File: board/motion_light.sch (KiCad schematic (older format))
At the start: 19 parts, among them CON1 AVR-ISP-6, J1 MOTION, J2 Conn_01x05, J3 USB_MICRO, J4 USB_MICRO, Q1 BSS83P, SW1 SW_Push, SW2 SW_Push, U1 ATTINY84A-SSU, U2 APA102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

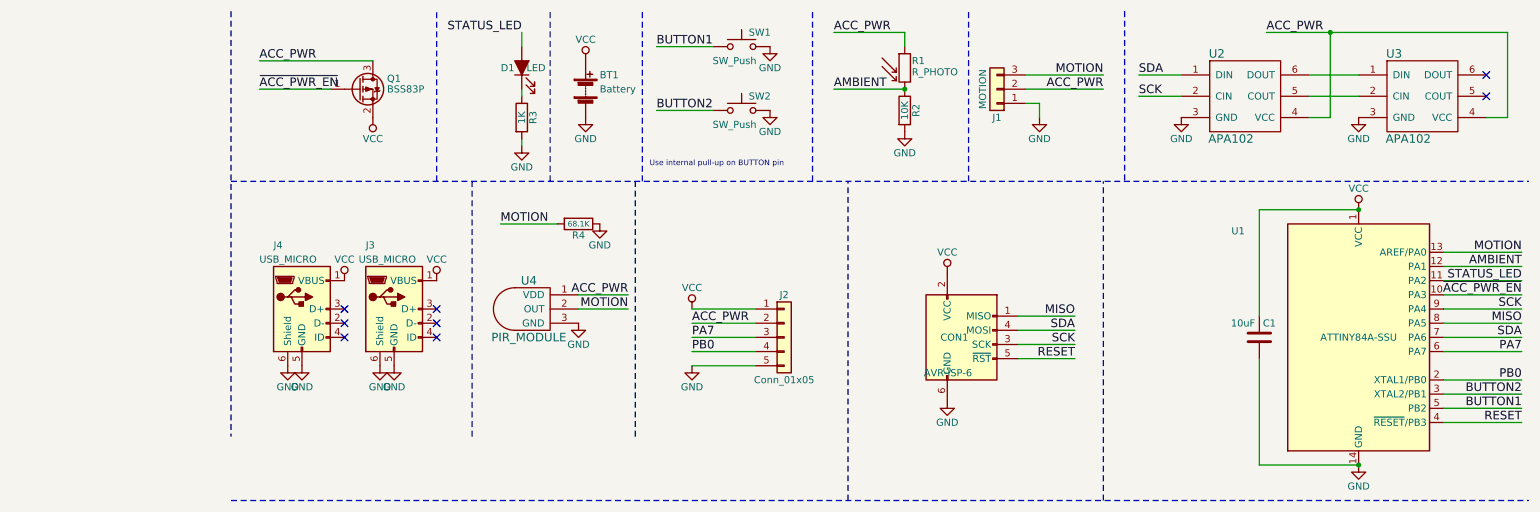
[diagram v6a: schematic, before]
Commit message: Add separate power control for motion detector power
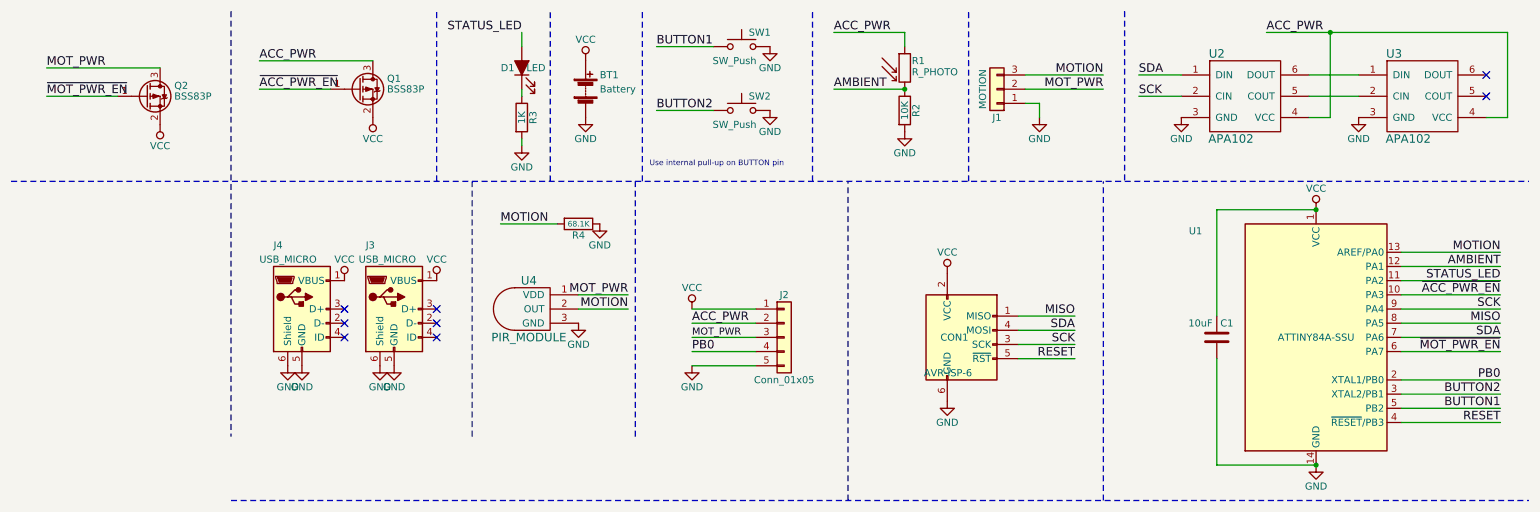
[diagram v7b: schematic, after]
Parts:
- added Q2: BSS83P, Package_TO_SOT_SMD:SOT-23, symbol Transistor_FET:BSS83P
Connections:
- net ACC_PWR: no longer J1.2 (Pin_2), U4.1 (VDD)
- net VCC: now also Q2.2 (S)
- net PA7 renamed MOT_PWR
- net MOT_PWR: now also J1.2 (Pin_2), U4.1 (VDD), Q2.3 (D); no longer U1.6 (PA7)
- new net ~MOT_PWR_EN: Q2.1 (G), U1.6 (PA7)
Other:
- moved on the sheet: C1, U1
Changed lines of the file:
@@
 L MCU_Microchip_ATtiny:ATtiny84A-SSU U1
 U 1 1 59B43E7D
-P 10000 2800
-F 0 "U1" H 9150 3550 50  0000 C CNN
-F 1 "ATTINY84A-SSU" H 10000 2800 50  0000 C CNN
-F 2 "Package_SO:SOIC-14_3.9x8.7mm_P1.27mm" H 10000 2600 50  0001 C CIN
-F 3 "http://www.microchip.com/mymicrochip/filehandler.aspx?ddocname=en590190" H 10000 2800 50  0001 C CNN
-F 4 "Microchip Technology" H 450 200 50  0001 C CNN "MFR"
-F 5 "ATTINY84A-SSUR" H 450 200 50  0001 C CNN "MPN"
-F 6 "Digikey" H 450 200 50  0001 C CNN "SPR"
-F 7 "ATTINY84A-SSURCT-ND" H 450 200 50  0001 C CNN "SPN"
-F 8 "-" H 450 200 50  0001 C CNN "SPURL"
-	1    10000 2800
+P 9700 2800
+F 0 "U1" H 8850 3550 50  0000 C CNN
+F 1 "ATTINY84A-SSU" H 9700 2800 50  0000 C CNN
+F 2 "Package_SO:SOIC-14_3.9x8.7mm_P1.27mm" H 9700 2600 50  0001 C CIN
+F 3 "http://www.microchip.com/mymicrochip/filehandler.aspx?ddocname=en590190" H 9700 2800 50  0001 C CNN
+F 4 "Microchip Technology" H 150 200 50  0001 C CNN "MFR"
+F 5 "ATTINY84A-SSUR" H 150 200 50  0001 C CNN "MPN"
+F 6 "Digikey" H 150 200 50  0001 C CNN "SPR"
+F 7 "ATTINY84A-SSURCT-ND" H 150 200 50  0001 C CNN "SPN"
+F 8 "-" H 150 200 50  0001 C CNN "SPURL"
+	1    9700 2800
 	1    0    0    -1
 $EndComp
@@
 L power:VCC #PWR02
 U 1 1 59B443A5
-P 10000 1900
-F 0 "#PWR02" H 10000 1750 50  0001 C CNN
-F 1 "VCC" H 10000 2050 50  0000 C CNN
-F 2 "" H 10000 1900 50  0001 C CNN
-F 3 "" H 10000 1900 50  0001 C CNN
-	1    10000 1900
+P 9700 1900
+F 0 "#PWR02" H 9700 1750 50  0001 C CNN
+F 1 "VCC" H 9700 2050 50  0000 C CNN
+F 2 "" H 9700 1900 50  0001 C CNN
+F 3 "" H 9700 1900 50  0001 C CNN
+	1    9700 1900
 	1    0    0    -1
 $EndComp
@@
 L power:GND #PWR03
 U 1 1 59B443C3
-P 10000 3700
-F 0 "#PWR03" H 10000 3450 50  0001 C CNN
-F 1 "GND" H 10000 3550 50  0000 C CNN
-F 2 "" H 10000 3700 50  0001 C CNN
-F 3 "" H 10000 3700 50  0001 C CNN
-	1    10000 3700
+P 9700 3700
+F 0 "#PWR03" H 9700 3450 50  0001 C CNN
+F 1 "GND" H 9700 3550 50  0000 C CNN
+F 2 "" H 9700 3700 50  0001 C CNN
+F 3 "" H 9700 3700 50  0001 C CNN
+	1    9700 3700
 	1    0    0    -1
 $EndComp
@@
 Text Label 5050 750  0    60   ~ 0
 BUTTON1
-Text Label 11150 2600 2    60   ~ 0
+Text Label 11000 2600 2    60   ~ 0
 SCK
 Text Label 8450 950  0    60   ~ 0
@@
 Text Label 8450 1100 0    60   ~ 0
 SCK
-Text Label 11150 2800 2    60   ~ 0
+Text Label 11000 2800 2    60   ~ 0
 SDA
-Text Label 11150 3300 2    60   ~ 0
+Text Label 11000 3300 2    60   ~ 0
 BUTTON1
 Text Label 8200 950  2    60   ~ 0
 MOTION
-Text Label 11150 2200 2    60   ~ 0
+Text Label 11000 2200 2    60   ~ 0
 MOTION
 Text Label 8000 2650 2    60   ~ 0
@@
 Text Label 8000 2950 2    60   ~ 0
 RESET
-Text Label 11150 3400 2    60   ~ 0
+Text Label 11000 3400 2    60   ~ 0
 RESET
-Text Label 11150 2700 2    60   ~ 0
+Text Label 11000 2700 2    60   ~ 0
 MISO
 Text Label 6300 1050 0    60   ~ 0
 AMBIENT
-Text Label 11150 2300 2    60   ~ 0
+Text Label 11000 2300 2    60   ~ 0
 AMBIENT
-Text Label 5300 2800 0    60   ~ 0
-PA7
 Text Label 5300 2900 0    60   ~ 0
 PB0
-Text Label 11150 3100 2    60   ~ 0
+Text Label 11000 3100 2    60   ~ 0
 PB0
-Text Label 11150 2900 2    60   ~ 0
-PA7
-Text Label 11150 2500 2    60   ~ 0
+Text Label 11000 2900 2    60   ~ 0
+~MOT_PWR_EN
+Text Label 11000 2500 2    60   ~ 0
 ~ACC_PWR_EN
-Text Label 11150 2400 2    60   ~ 0
+Text Label 11000 2400 2    60   ~ 0
 STATUS_LED
 Text Notes 5000 1600 0    39   ~ 0
@@
 Text Label 5050 1200 0    60   ~ 0
 BUTTON2
-Text Label 11150 3200 2    60   ~ 0
+Text Label 11000 3200 2    60   ~ 0
 BUTTON2
 Text Label 3950 2000 0    60   ~ 0
@@
 L Device:C C1
 U 1 1 5A38B28C
-P 9300 2800
-F 0 "C1" H 9325 2900 50  0000 L CNN
-F 1 "10uF" H 9100 2900 50  0000 L CNN
-F 2 "Capacitor_SMD:C_0805_2012Metric_Pad1.15x1.40mm_HandSolder" H 9338 2650 50  0001 C CNN
-F 3 "" H 9300 2800 50  0001 C CNN
-	1    9300 2800
+P 9000 2800
+F 0 "C1" H 9025 2900 50  0000 L CNN
+F 1 "10uF" H 8800 2900 50  0000 L CNN
+F 2 "Capacitor_SMD:C_0805_2012Metric_Pad1.15x1.40mm_HandSolder" H 9038 2650 50  0001 C CNN
+F 3 "" H 9000 2800 50  0001 C CNN
+	1    9000 2800
 	1    0    0    -1
 $EndComp
@@
 	5450 750  5050 750
 Wire Wire Line
-	10600 2600 11150 2600
+	10300 2600 11000 2600
 Wire Wire Line
 	9650 1100 10000 1100
@@
 	8750 1100 8450 1100
 Wire Wire Line
-	10600 2800 11150 2800
-Wire Wire Line
-	10600 3300 11150 3300
+	10300 2800 11000 2800
+Wire Wire Line
+	10300 3300 11000 3300
 Wire Wire Line
 	11050 1250 11050 650
@@
 	7750 1150 7750 1250
 Wire Wire Line
-	10600 2200 11150 2200
-Wire Wire Line
-	10600 3400 11150 3400
-Wire Wire Line
-	10600 2700 11150 2700
+	10300 2200 11000 2200
+Wire Wire Line
+	10300 3400 11000 3400
+Wire Wire Line
+	10300 2700 11000 2700
 Wire Wire Line
 	6800 1050 6300 1050
 Wire Wire Line
-	10600 2300 11150 2300
-Wire Notes Line
-	2050 1700 11200 1700
+	10300 2300 11000 2300
 Wire Notes Line
 	7250 1700 7250 500
@@
 	5750 2700 5300 2700
 Wire Wire Line
-	10600 2400 11150 2400
-Wire Wire Line
-	10600 2500 11150 2500
-Wire Wire Line
-	10600 2900 11150 2900
-Wire Wire Line
-	10600 3100 11150 3100
-Wire Wire Line
-	10600 3200 11150 3200
+	10300 2400 11000 2400
+Wire Wire Line
+	10300 2500 11000 2500
+Wire Wire Line
+	10300 2900 11000 2900
+Wire Wire Line
+	10300 3100 11000 3100
+Wire Wire Line
+	10300 3200 11000 3200
 Wire Notes Line
 	4900 3500 4900 1700
@@
 	4500 2500 4850 2500
 Text Label 4850 2500 2    60   ~ 0
-ACC_PWR
+MOT_PWR
 Text Label 8200 1050 2    60   ~ 0
-ACC_PWR
+MOT_PWR
 $Comp
 L Connector:USB_B_Micro J3
@@
 $EndComp
 Wire Wire Line
-	9300 1900 9300 2650
-Wire Wire Line
-	9300 1900 10000 1900
-Connection ~ 10000 1900
-Wire Wire Line
-	10000 3700 9300 3700
-Wire Wire Line
-	9300 3700 9300 2950
-Connection ~ 10000 3700
+	9000 1900 9000 2650
+Wire Wire Line
+	9000 1900 9700 1900
+Connection ~ 9700 1900
+Wire Wire Line
+	9700 3700 9000 3700
+Wire Wire Line
+	9000 3700 9000 2950
+Connection ~ 9700 3700
 Wire Wire Line
 	7600 2850 8000 2850
@@
 Wire Wire Line
 	8000 2750 7600 2750
+Text Label 750  1100 0    60   ~ 0
+~MOT_PWR_EN
+Wire Wire Line
+	1250 1100 750  1100
+Wire Wire Line
+	1550 900  750  900
+Text Label 750  900  0    60   ~ 0
+MOT_PWR
+$Comp
+L Transistor_FET:BSS83P Q2
+U 1 1 5B7A3B7E
+P 1450 1100
+F 0 "Q2" H 1650 1175 50  0000 L CNN
+F 1 "BSS83P" H 1650 1100 50  0000 L CNN
+F 2 "Package_TO_SOT_SMD:SOT-23" H 1650 1025 50  0001 L CIN
+F 3 "" H 1450 1100 50  0001 L CNN
+	1    1450 1100
+	1    0    0    -1
+$EndComp
+$Comp
+L power:VCC #PWR0104
+U 1 1 5B7A3B85
+P 1550 1300
+F 0 "#PWR0104" H 1550 1150 50  0001 C CNN
+F 1 "VCC" H 1550 1450 50  0000 C CNN
+F 2 "" H 1550 1300 50  0001 C CNN
+F 3 "" H 1550 1300 50  0001 C CNN
+	1    1550 1300
+	-1   0    0    1
+$EndComp
+Wire Notes Line
+	500  1700 11200 1700
+Text Label 5300 2800 0    50   ~ 0
+MOT_PWR
 $EndSCHEMATC

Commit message: Update board BoM; upgrade symbols
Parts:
- C1: MFR (none) -> Samsung Electro-Mechanics; MPN (none) -> CL21A106KQCLRNC; SPN (none) -> 1276-2405-1-ND; SPR (none) -> Digikey; SPURL (none) -> -
- D1: SPN - -> 732-4985-1-ND; SPR - -> Digikey
- J3, J4: MFR (none) -> -; MPN (none) -> -; SPN (none) -> -; SPR (none) -> -; SPURL (none) -> -
- Q1, Q2: MFR (none) -> Infineon Technologies; MPN (none) -> BSS83PH6327XTSA1; SPN (none) -> BSS83PH6327XTSA1CT-ND; SPR (none) -> Digikey; SPURL (none) -> -
- U1: symbol MCU_Microchip_ATtiny:ATtiny84A-SSU -> motion_light-rescue:ATtiny84A-SSU-MCU_Microchip_ATtiny
- U2, U3: MPN APA102C -> SK9822; SPN - -> SK9822
- U4: MPN EKMC1603112 -> EKMC1604112; SPN 255-3087-ND -> 255-5709-ND
